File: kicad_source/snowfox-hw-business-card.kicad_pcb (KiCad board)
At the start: 2 copper layers, 85 x 54 mm, 104 parts, among them CN1 Micro_SDCard, CN2 CONN_02X05, CN3 CONN_01X24, CN4 USB_OTG, CN5 CONN_01X04, CN6 CONN_01X04, Q1 SI1304BDL, Q2 BC847, SW1 TAST_VER, SW2 TAST_VER, SW3 TAST_VER, SW4 TAST_VER, SW5 SWITCH_INV, U1 W25Q80D, U2 ATECC608A, U3 FE310-G002, U4 FT230XS, U5 TPS736XX, U6 TPS736XX, U7 M24LR, Y1 16MHz

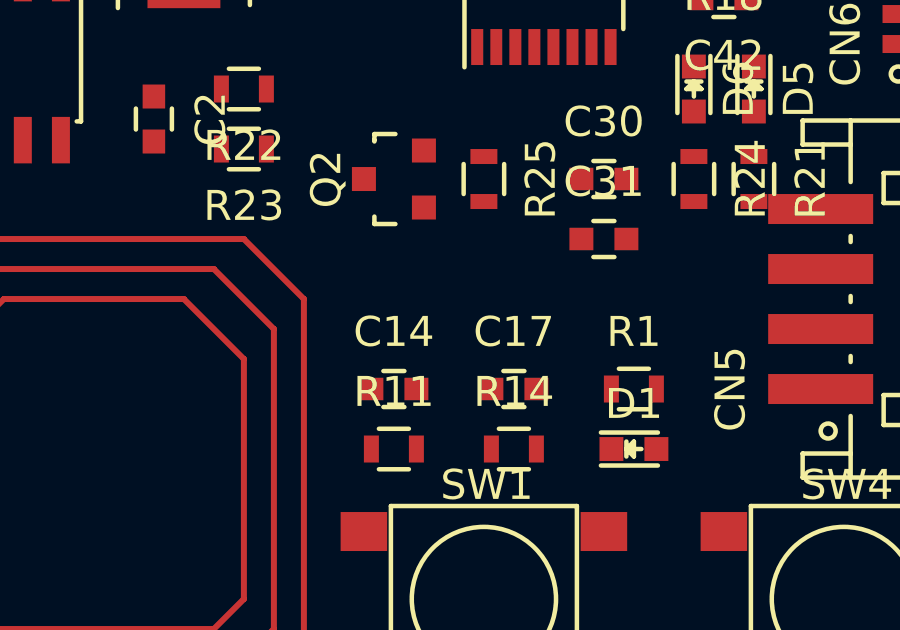
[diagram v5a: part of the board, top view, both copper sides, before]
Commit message: added BMA400 accelerometer
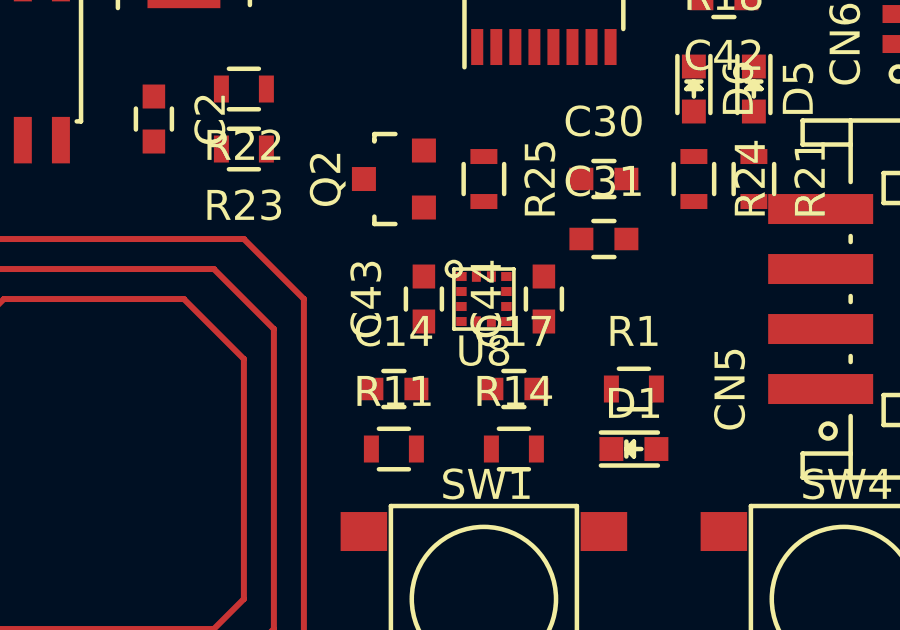
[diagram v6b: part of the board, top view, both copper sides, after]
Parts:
- added C43: 100n, capacitors:C_0603, F.Cu at (142.0, 123.0)
- added C44: 100n, capacitors:C_0603, F.Cu at (146.0, 123.0)
- added U8: BMA400, IC_sensor:BMA400, F.Cu at (144.0, 123.0)

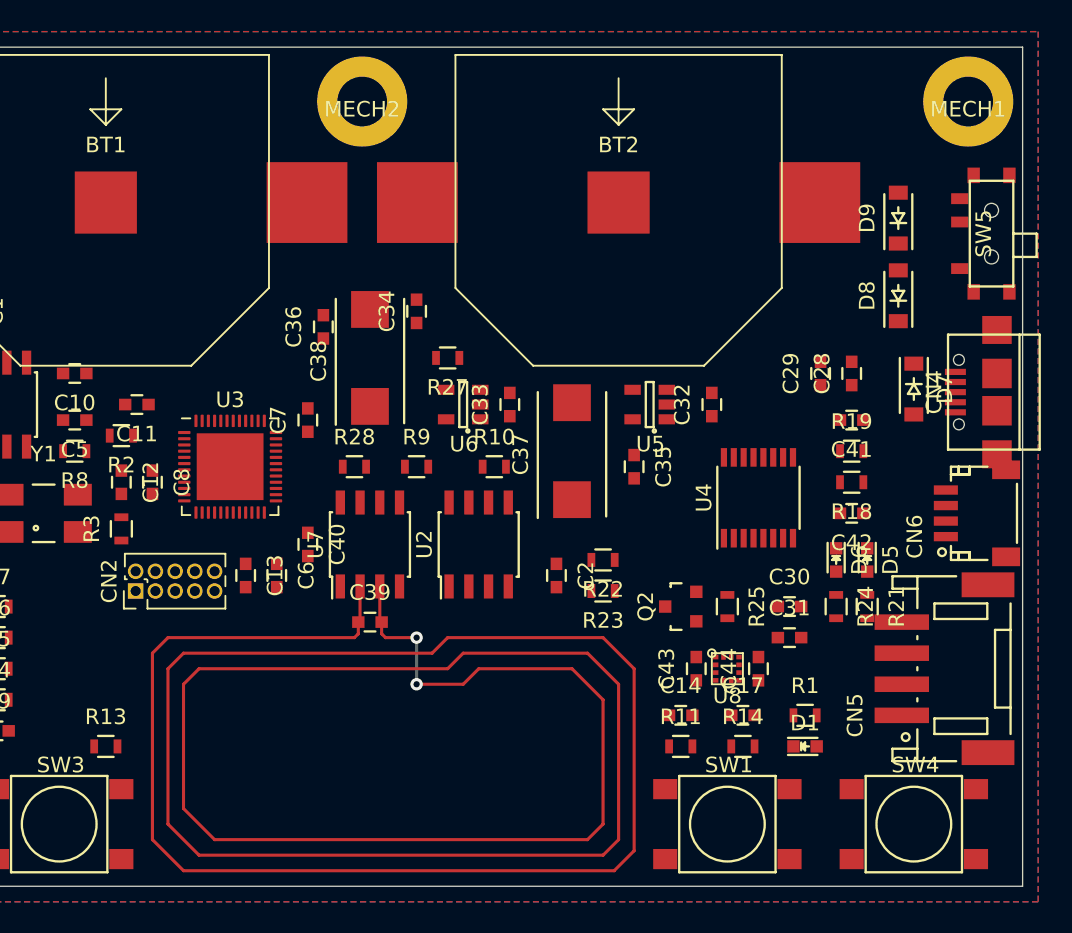
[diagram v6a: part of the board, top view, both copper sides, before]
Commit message: changed JTAG connector
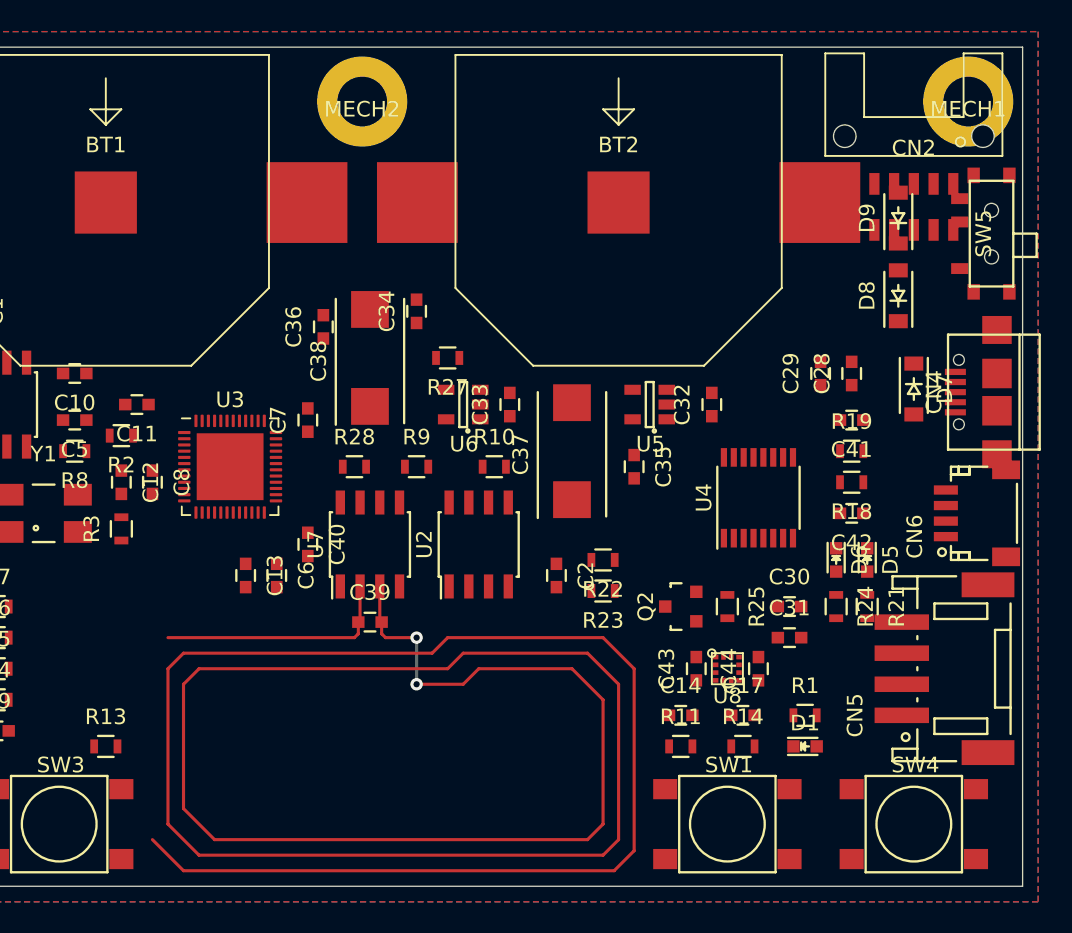
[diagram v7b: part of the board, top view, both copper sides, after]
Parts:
- CN2: footprint pin_headers:Pin_Header_Straight_2x05_Pitch1.27mm -> CON_samtec:FSH-105-04-L-DH-SL
- moved CN2 57.4 mm to (156.0, 90.0), turned to 180 degrees
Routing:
- net /NFC/ANTENNA: track 250.4 -> 237.0 mm

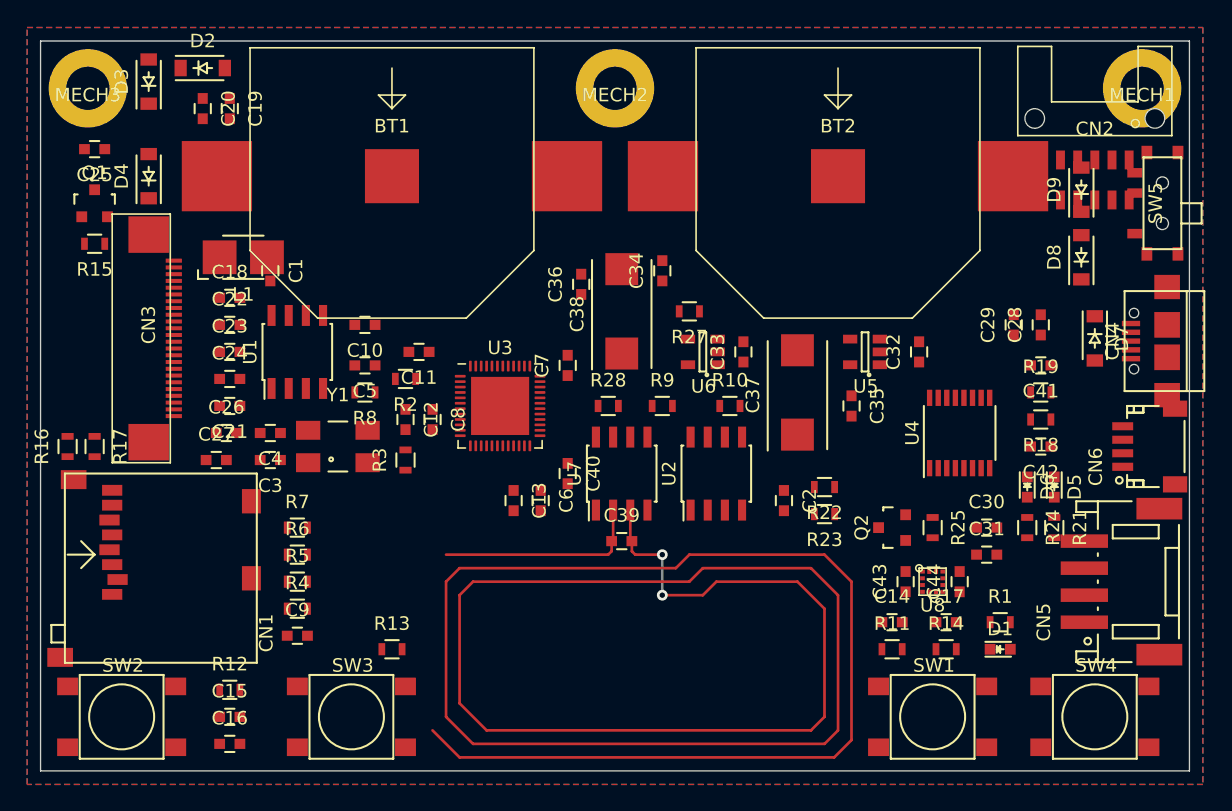
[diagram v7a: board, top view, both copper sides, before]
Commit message: used small side switch for reset, added expansion connector,changed mounting holes
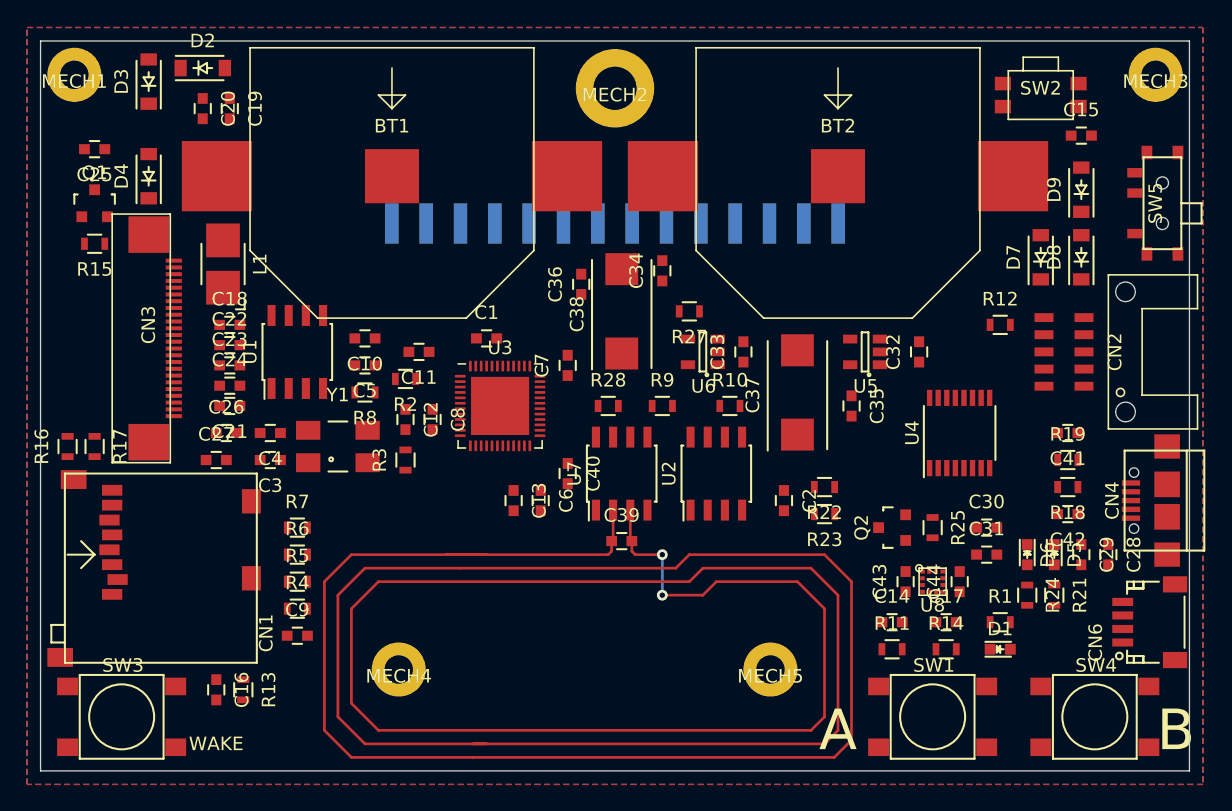
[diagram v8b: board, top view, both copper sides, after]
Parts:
- added MECH4: MHNP_2.1_4.0, MECH_mounting_holes:MH_210_400_NP, F.Cu at (104.5, 129.5)
- added MECH5: MHNP_2.1_4.0, MECH_mounting_holes:MH_210_400_NP, F.Cu at (132.0, 129.5)
- CN5: value CONN_01X04 -> CONN_01X14; footprint connectors_JST_PH:Connectors_JST_S4B-PH-SM4-TB -> CON_samtec:SIB-114-02-F-S_MATING; moved to B.Cu
- MECH1, MECH3: value MHP_3.2_5.8 -> MHNP_2.1_4.0; footprint MECH_mounting_holes:MHP_3.2_5.8 -> MECH_mounting_holes:MH_210_400_NP
- SW2: footprint mechanical-switches:WE_430182050816 -> mechanical-switches:WE_434351045816
- moved SW2 82.1 mm to (152.0, 87.0), turned to 180 degrees
- moved MECH1 79.0 mm to (80.5, 85.5)
- moved MECH3 79.0 mm to (160.5, 85.5)
- moved C15 76.3 mm to (155.0, 90.0)
- moved R12 63.1 mm to (149.0, 104.0)
- moved CN5 45.9 mm to (120.5, 96.5), turned to 0 degrees
- moved C28 17.7 mm to (157.0, 121.0), turned to 270 degrees
- moved C29 17.7 mm to (155.0, 121.0), turned to 270 degrees
- moved SW3 17.0 mm to (84.0, 133.0)
- moved C1 16.8 mm to (111.0, 105.0), turned to 0 degrees
- moved CN2 16.0 mm to (157.0, 106.0), turned to 90 degrees
- moved CN6 13.0 mm to (160.0, 126.0)
- moved CN4 11.8 mm to (158.0, 117.0)
- moved R13 11.4 mm to (93.0, 131.0), turned to 270 degrees
- moved D7 7.21 mm to (152.0, 99.0), turned to 90 degrees
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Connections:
- CN5 pad 1: /Microcontroller/EXT_RX -> (no net)
- CN5 pad 2: /Microcontroller/EXT_TX -> /Microcontroller/BUTTON_A
- CN5 pad 3: +3V3 -> /Microcontroller/BUTTON_B
- CN5 pad 4: GND -> /Microcontroller/LED
- U3 pad 26: (no net) -> /Microcontroller/GPIO_1
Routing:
- net /NFC/ANTENNA: track 237.0 -> 300.7 mm
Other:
- board text added: "A"
- board text added: "B"
- board text added: "WAKE"
